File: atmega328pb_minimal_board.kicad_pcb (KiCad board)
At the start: 2 copper layers, 54 x 33.7 mm, 14 parts, among them J1 Conn_01x02_Male, J2 Conn_02x05_Odd_Even, J3 Conn_01x16_Male, J4 Conn_01x16_Male, J5 Conn_01x02_Male, SW1 Reset, U1 ATmega328PB-AU, Y1 16MHz

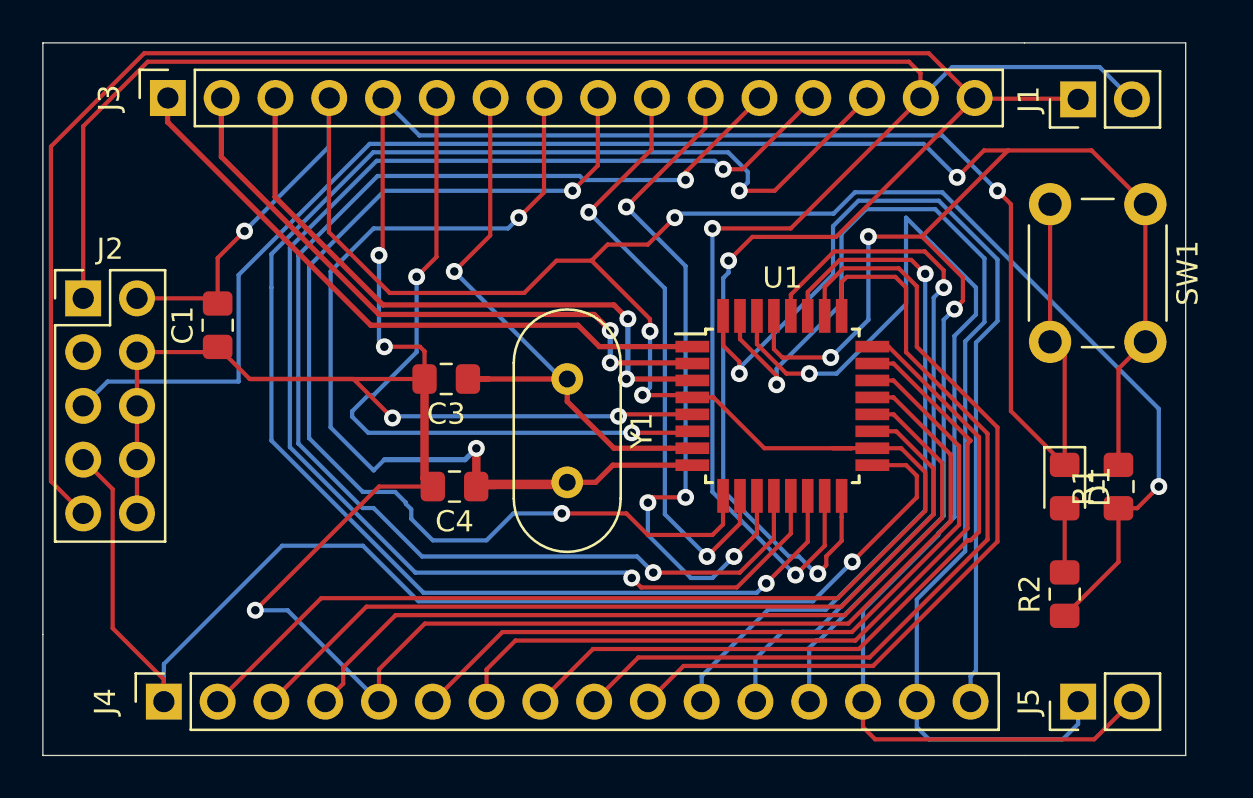
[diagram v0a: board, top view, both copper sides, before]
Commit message: add some pin labels
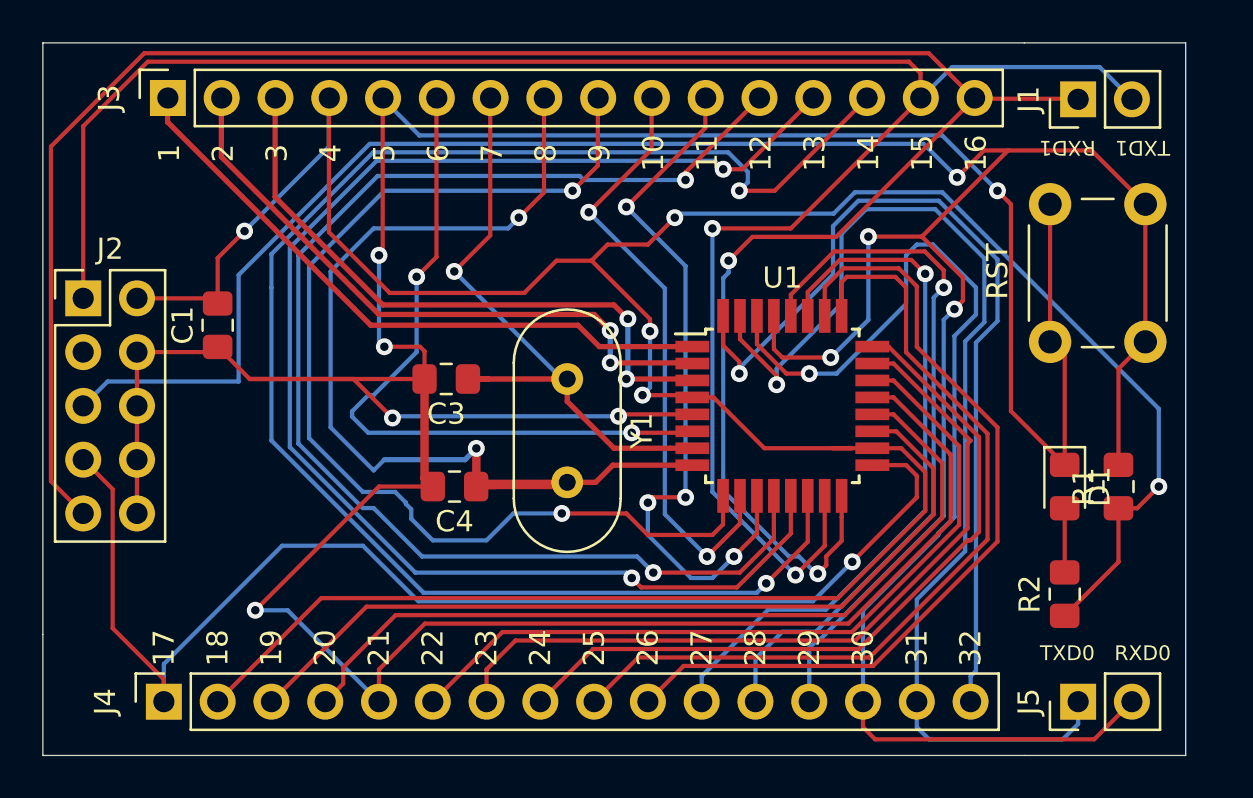
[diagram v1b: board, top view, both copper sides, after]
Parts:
- removed SW1: Reset, Button_Switch_THT:SW_PUSH_6mm_H5mm
- added RST: Reset, Button_Switch_THT:SW_PUSH_6mm_H5mm, F.Cu at (83.2, 32.4)
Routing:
- net PIN30: track 55.7 -> 53.6 mm
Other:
- board text added: "1"
- board text added: "10"
- board text added: "11"
- board text added: "12"
- board text added: "13"
- board text added: "14"
- board text added: "15"
- board text added: "16"
- board text added: "17"
- board text added: "18"
- board text added: "19"
- board text added: "2"
- board text added: "20"
- board text added: "21"
- board text added: "22"
- board text added: "23"
- board text added: "24"
- board text added: "25"
- board text added: "26"
- board text added: "27"
- board text added: "28"
- board text added: "29"
- board text added: "3"
- board text added: "30"
- board text added: "31"
- board text added: "32"
- board text added: "4"
- board text added: "5"
- board text added: "6"
- board text added: "7"
- board text added: "8"
- board text added: "9"
- board text added: "RXD0"
- board text added: "RXD1"
- board text added: "TXD0"
- board text added: "TXD1"
- board text added: "Yovan Naumovski - 2019 Atmega328PB Miniboard v0.1"
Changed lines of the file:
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@@
   (general
     (thickness 1.6)
-    (drawings 7)
-    (tracks 496)
+    (drawings 44)
+    (tracks 497)
     (zones 0)
     (modules 14)
@@
   )
   (setup
-    (last_trace_width 0.4)
+    (last_trace_width 0.2)
     (user_trace_width 0.2)
     (user_trace_width 0.4)
@@
     (descr "tactile push button, 6x6mm e.g. PHAP33xx series, height=5mm")
     (tags "tact sw push 6mm")
-    (fp_text reference SW1 (at 3.25 -2 90) (layer F.SilkS)
+    (fp_text reference RST (at 3.175 6.985 90) (layer F.SilkS)
       (effects (font (size 1 1) (thickness 0.15)))
     )
@@
       (rotate (xyz 0 0 0))
     )
+  )
+  (gr_text "Yovan Naumovski - 2019\nAtmega328PB Miniboard v0.1" (at 51.054 52.07) (layer B.SilkS)
+    (effects (font (size 0.7 0.7) (thickness 0.15)) (justify mirror))
+  )
+  (gr_text TXD1 (at 83.058 29.718 180) (layer F.SilkS)
+    (effects (font (size 0.7 0.7) (thickness 0.15)))
+  )
+  (gr_text RXD1 (at 79.502 29.718 180) (layer F.SilkS)
+    (effects (font (size 0.7 0.7) (thickness 0.15)))
+  )
+  (gr_text TXD0 (at 79.502 53.594) (layer F.SilkS)
+    (effects (font (size 0.7 0.7) (thickness 0.15)))
+  )
+  (gr_text RXD0 (at 83.058 53.594) (layer F.SilkS)
+    (effects (font (size 0.7 0.7) (thickness 0.15)))
+  )
+  (gr_text 32 (at 74.93 53.34 90) (layer F.SilkS)
+    (effects (font (size 1 1) (thickness 0.25)))
+  )
+  (gr_text 31 (at 72.39 53.34 90) (layer F.SilkS)
+    (effects (font (size 1 1) (thickness 0.25)))
+  )
+  (gr_text 30 (at 69.85 53.34 90) (layer F.SilkS)
+    (effects (font (size 1 1) (thickness 0.25)))
+  )
+  (gr_text 29 (at 67.31 53.34 90) (layer F.SilkS)
+    (effects (font (size 1 1) (thickness 0.25)))
+  )
+  (gr_text 28 (at 64.77 53.34 90) (layer F.SilkS)
+    (effects (font (size 1 1) (thickness 0.25)))
+  )
+  (gr_text 27 (at 62.23 53.34 90) (layer F.SilkS)
+    (effects (font (size 1 1) (thickness 0.25)))
+  )
+  (gr_text 26 (at 59.69 53.34 90) (layer F.SilkS)
+    (effects (font (size 1 1) (thickness 0.25)))
+  )
+  (gr_text 25 (at 57.15 53.34 90) (layer F.SilkS)
+    (effects (font (size 1 1) (thickness 0.25)))
+  )
+  (gr_text 24 (at 54.61 53.34 90) (layer F.SilkS)
+    (effects (font (size 1 1) (thickness 0.25)))
+  )
+  (gr_text 23 (at 52.07 53.34 90) (layer F.SilkS)
+    (effects (font (size 1 1) (thickness 0.25)))
+  )
+  (gr_text 22 (at 49.53 53.34 90) (layer F.SilkS)
+    (effects (font (size 1 1) (thickness 0.25)))
+  )
+  (gr_text 21 (at 46.99 53.34 90) (layer F.SilkS)
+    (effects (font (size 1 1) (thickness 0.25)))
+  )
+  (gr_text 20 (at 44.45 53.34 90) (layer F.SilkS)
+    (effects (font (size 1 1) (thickness 0.25)))
+  )
+  (gr_text 19 (at 41.91 53.34 90) (layer F.SilkS)
+    (effects (font (size 1 1) (thickness 0.25)))
+  )
+  (gr_text 18 (at 39.37 53.34 90) (layer F.SilkS)
+    (effects (font (size 1 1) (thickness 0.25)))
+  )
+  (gr_text 17 (at 36.83 53.34 90) (layer F.SilkS)
+    (effects (font (size 1 1) (thickness 0.25)))
+  )
+  (gr_text 16 (at 75.184 29.972 90) (layer F.SilkS)
+    (effects (font (size 1 1) (thickness 0.25)))
+  )
+  (gr_text 15 (at 72.644 29.972 90) (layer F.SilkS)
+    (effects (font (size 1 1) (thickness 0.25)))
+  )
+  (gr_text 14 (at 70.104 29.972 90) (layer F.SilkS)
+    (effects (font (size 1 1) (thickness 0.25)))
+  )
+  (gr_text 13 (at 67.564 29.972 90) (layer F.SilkS)
+    (effects (font (size 1 1) (thickness 0.25)))
+  )
+  (gr_text 12 (at 65.024 29.972 90) (layer F.SilkS)
+    (effects (font (size 1 1) (thickness 0.25)))
+  )
+  (gr_text 11 (at 62.484 29.972 90) (layer F.SilkS)
+    (effects (font (size 1 1) (thickness 0.25)))
+  )
+  (gr_text 10 (at 59.944 29.972 90) (layer F.SilkS)
+    (effects (font (size 1 1) (thickness 0.25)))
+  )
+  (gr_text 9 (at 57.404 29.972 90) (layer F.SilkS)
+    (effects (font (size 1 1) (thickness 0.25)))
+  )
+  (gr_text 8 (at 54.864 29.972 90) (layer F.SilkS)
+    (effects (font (size 1 1) (thickness 0.25)))
+  )
+  (gr_text 7 (at 52.324 29.972 90) (layer F.SilkS)
+    (effects (font (size 1 1) (thickness 0.25)))
+  )
+  (gr_text 6 (at 49.784 29.972 90) (layer F.SilkS)
+    (effects (font (size 1 1) (thickness 0.25)))
+  )
+  (gr_text 5 (at 47.244 29.972 90) (layer F.SilkS)
+    (effects (font (size 1 1) (thickness 0.25)))
+  )
+  (gr_text 4 (at 44.704 29.972 90) (layer F.SilkS)
+    (effects (font (size 1 1) (thickness 0.25)))
+  )
+  (gr_text 3 (at 42.164 29.972 90) (layer F.SilkS)
+    (effects (font (size 1 1) (thickness 0.25)))
+  )
+  (gr_text 2 (at 39.624 29.972 90) (layer F.SilkS)
+    (effects (font (size 1 1) (thickness 0.25)))
+  )
+  (gr_text 1 (at 37.084 29.972 90) (layer F.SilkS)
+    (effects (font (size 1 1) (thickness 0.25)))
   )
   (gr_line (start 85.09 58.42) (end 77.47 58.42) (layer Edge.Cuts) (width 0.05))
@@
   (segment (start 75.184 37.592) (end 75.184 36.322) (width 0.2) (layer B.Cu) (net 22))
   (segment (start 75.184 36.322) (end 73.152 34.29) (width 0.2) (layer B.Cu) (net 22))
-  (segment (start 73.152 34.29) (end 71.882 33.02) (width 0.2) (layer B.Cu) (net 22))
   (via (at 67.31 40.386) (size 0.8) (drill 0.4) (layers F.Cu B.Cu) (net 22))
   (segment (start 68.600002 40.386) (end 67.31 40.386) (width 0.2) (layer B.Cu) (net 22))
-  (segment (start 71.882 33.02) (end 71.882 37.104002) (width 0.2) (layer B.Cu) (net 22))
   (segment (start 71.882 37.104002) (end 68.600002 40.386) (width 0.2) (layer B.Cu) (net 22))
   (segment (start 64.84 38.66) (end 64.84 37.66) (width 0.2) (layer F.Cu) (net 22))
@@
   (segment (start 80.772 57.658) (end 82.55 55.88) (width 0.2) (layer F.Cu) (net 22))
   (segment (start 70.425919 57.658) (end 80.772 57.658) (width 0.2) (layer F.Cu) (net 22))
+  (segment (start 73.152 34.29) (end 72.39 34.29) (width 0.2) (layer B.Cu) (net 22))
+  (segment (start 72.39 34.29) (end 71.882 34.798) (width 0.2) (layer B.Cu) (net 22))
+  (segment (start 71.882 34.798) (end 71.882 37.084) (width 0.2) (layer B.Cu) (net 22))
   (segment (start 73.66 35.508349) (end 73.66 36.322) (width 0.2) (layer F.Cu) (net 23))
   (segment (start 72.765621 34.61397) (end 73.66 35.508349) (width 0.2) (layer F.Cu) (net 23))
